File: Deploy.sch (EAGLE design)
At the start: 41 parts, among them SW5 THAU13-AB-R, SW6 THAU13-AB-R, SW7 TVAF06-A020B-R, SW8 TVAF06-A020B-R, T2 HN1C01FU, T3 HN1C01FU, U4 OPA340N, U5 DRIVER-LV8548MC-AH(SOIC10), U6 I-02247_NJM2845

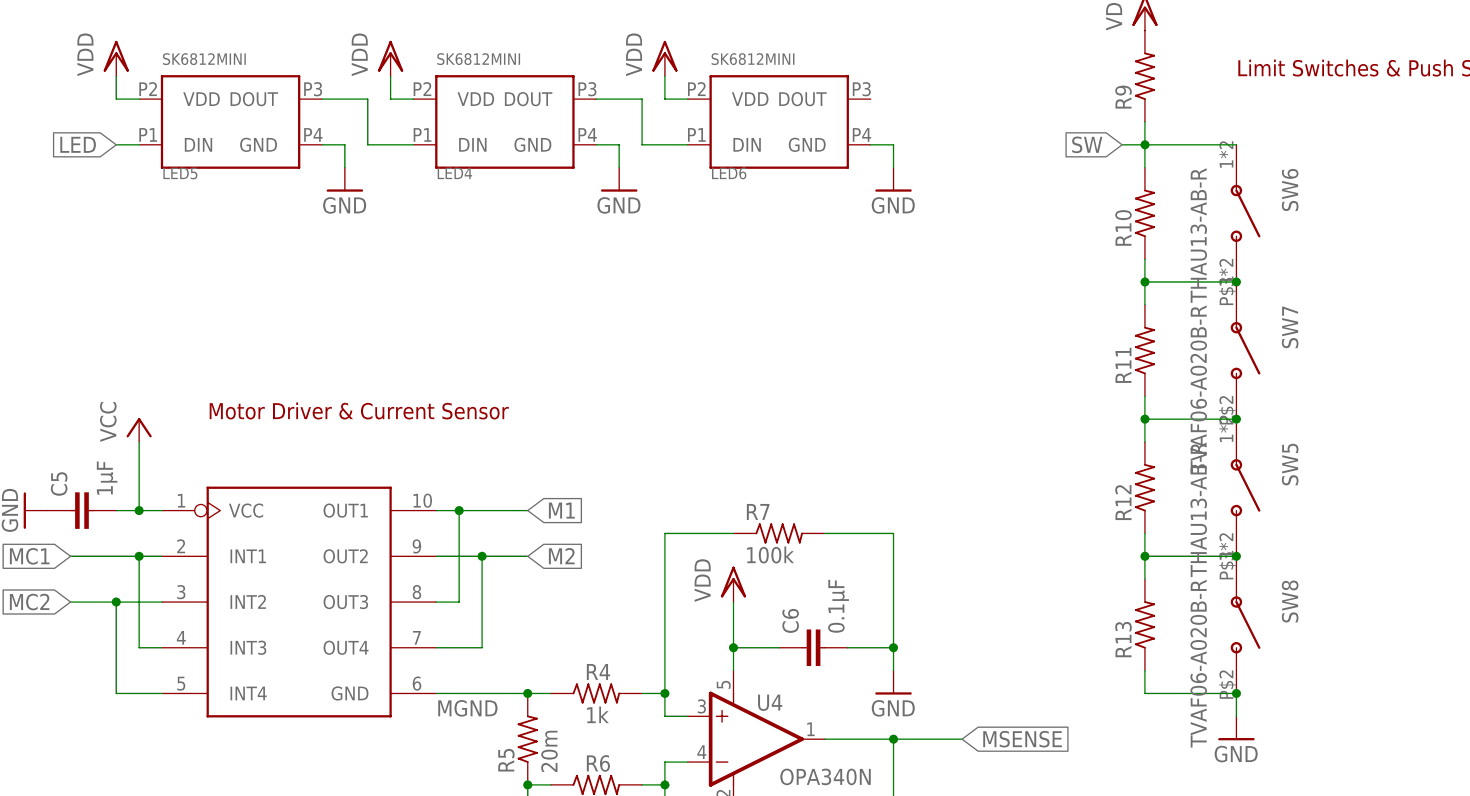
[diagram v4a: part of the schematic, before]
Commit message: Format silk
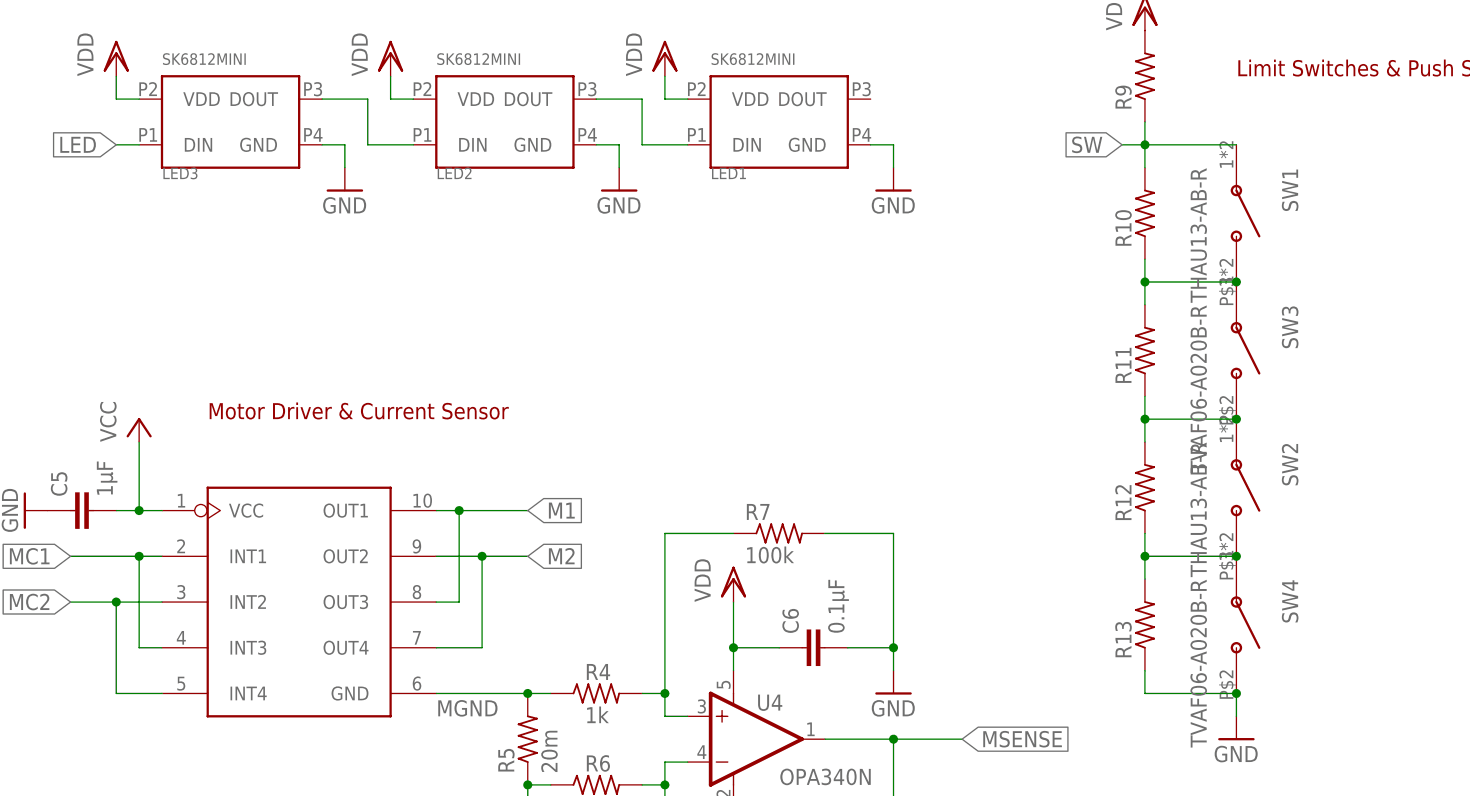
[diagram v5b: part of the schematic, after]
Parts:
- renumbered LED4 to LED2, LED5 to LED3, LED6 to LED1, SW5 to SW2, SW6 to SW1, SW7 to SW3, SW8 to SW4
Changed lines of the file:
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@@
 <part name="GND37" library="supply1" library_urn="urn:adsk.eagle:library:371" deviceset="GND" device=""/>
 <part name="R1" library="rcl" library_urn="urn:adsk.eagle:library:334" deviceset="R-US_" device="R0603" package3d_urn="urn:adsk.eagle:package:23555/3" value="100k"/>
-<part name="SW5" library="switches" deviceset="THAU13-AB-R" device=""/>
-<part name="SW6" library="switches" deviceset="THAU13-AB-R" device=""/>
+<part name="SW2" library="switches" deviceset="THAU13-AB-R" device=""/>
+<part name="SW1" library="switches" deviceset="THAU13-AB-R" device=""/>
 <part name="C4" library="rcl" library_urn="urn:adsk.eagle:library:334" deviceset="C-EU" device="C0603" package3d_urn="urn:adsk.eagle:package:23616/2" value="0.1µF"/>
 <part name="GND38" library="supply1" library_urn="urn:adsk.eagle:library:371" deviceset="GND" device=""/>
-<part name="LED4" library="leds" deviceset="SK6812MINI" device=""/>
-<part name="LED5" library="leds" deviceset="SK6812MINI" device=""/>
+<part name="LED2" library="leds" deviceset="SK6812MINI" device=""/>
+<part name="LED3" library="leds" deviceset="SK6812MINI" device=""/>
 <part name="VDD13" library="supply1" library_urn="urn:adsk.eagle:library:371" deviceset="VDD" device=""/>
 <part name="VDD14" library="supply1" library_urn="urn:adsk.eagle:library:371" deviceset="VDD" device=""/>
 <part name="GND39" library="supply1" library_urn="urn:adsk.eagle:library:371" deviceset="GND" device=""/>
 <part name="GND40" library="supply1" library_urn="urn:adsk.eagle:library:371" deviceset="GND" device=""/>
-<part name="SW7" library="switches" deviceset="TVAF06-A020B-R" device=""/>
-<part name="LED6" library="leds" deviceset="SK6812MINI" device=""/>
+<part name="SW3" library="switches" deviceset="TVAF06-A020B-R" device=""/>
+<part name="LED1" library="leds" deviceset="SK6812MINI" device=""/>
 <part name="GND41" library="supply1" library_urn="urn:adsk.eagle:library:371" deviceset="GND" device=""/>
 <part name="VDD15" library="supply1" library_urn="urn:adsk.eagle:library:371" deviceset="VDD" device=""/>
@@
 <part name="VDD16" library="supply1" library_urn="urn:adsk.eagle:library:371" deviceset="VDD" device=""/>
 <part name="GND42" library="supply1" library_urn="urn:adsk.eagle:library:371" deviceset="GND" device=""/>
-<part name="SW8" library="switches" deviceset="TVAF06-A020B-R" device=""/>
+<part name="SW4" library="switches" deviceset="TVAF06-A020B-R" device=""/>
 </parts>
 <sheets>
@@
 <attribute name="VALUE" x="69.85" y="155.702" size="1.778" layer="96" rot="R180"/>
 </instance>
-<instance part="SW5" gate="G$1" x="254" y="114.3" smashed="yes" rot="R270">
+<instance part="SW2" gate="G$1" x="254" y="114.3" smashed="yes" rot="R270">
 <attribute name="NAME" x="259.08" y="119.38" size="1.778" layer="95" rot="R270"/>
 <attribute name="VALUE" x="248.92" y="119.38" size="1.778" layer="96" rot="R270"/>
 </instance>
-<instance part="SW6" gate="G$1" x="254" y="144.78" smashed="yes" rot="R270">
+<instance part="SW1" gate="G$1" x="254" y="144.78" smashed="yes" rot="R270">
 <attribute name="NAME" x="259.08" y="149.86" size="1.778" layer="95" rot="R270"/>
 <attribute name="VALUE" x="248.92" y="149.86" size="1.778" layer="96" rot="R270"/>
@@
 <attribute name="VALUE" x="-15.24" y="55.88" size="1.778" layer="96"/>
 </instance>
-<instance part="LED4" gate="G$1" x="172.72" y="154.94" smashed="yes" rot="MR180">
+<instance part="LED2" gate="G$1" x="172.72" y="154.94" smashed="yes" rot="MR180">
 <attribute name="NAME" x="165.1" y="149.86" size="1.27" layer="95" rot="MR180"/>
 <attribute name="VALUE" x="165.1" y="162.56" size="1.27" layer="96" rot="MR180"/>
 </instance>
-<instance part="LED5" gate="G$1" x="142.24" y="154.94" smashed="yes" rot="MR180">
+<instance part="LED3" gate="G$1" x="142.24" y="154.94" smashed="yes" rot="MR180">
 <attribute name="NAME" x="134.62" y="149.86" size="1.27" layer="95" rot="MR180"/>
 <attribute name="VALUE" x="134.62" y="162.56" size="1.27" layer="96" rot="MR180"/>
@@
 <attribute name="VALUE" x="182.88" y="144.78" size="1.778" layer="96"/>
 </instance>
-<instance part="SW7" gate="G$1" x="254" y="129.54" smashed="yes" rot="R270">
+<instance part="SW3" gate="G$1" x="254" y="129.54" smashed="yes" rot="R270">
 <attribute name="NAME" x="259.08" y="134.62" size="1.778" layer="95" rot="R270"/>
 <attribute name="VALUE" x="248.92" y="134.62" size="1.778" layer="96" rot="R270"/>
 </instance>
-<instance part="LED6" gate="G$1" x="203.2" y="154.94" smashed="yes" rot="MR180">
+<instance part="LED1" gate="G$1" x="203.2" y="154.94" smashed="yes" rot="MR180">
 <attribute name="NAME" x="195.58" y="149.86" size="1.27" layer="95" rot="MR180"/>
 <attribute name="VALUE" x="195.58" y="162.56" size="1.27" layer="96" rot="MR180"/>
@@
 <attribute name="VALUE" x="251.46" y="83.82" size="1.778" layer="96"/>
 </instance>
-<instance part="SW8" gate="G$1" x="254" y="99.06" smashed="yes" rot="R270">
+<instance part="SW4" gate="G$1" x="254" y="99.06" smashed="yes" rot="R270">
 <attribute name="NAME" x="259.08" y="104.14" size="1.778" layer="95" rot="R270"/>
 <attribute name="VALUE" x="248.92" y="104.14" size="1.778" layer="96" rot="R270"/>
@@
 </segment>
 <segment>
-<pinref part="LED5" gate="G$1" pin="GND"/>
+<pinref part="LED3" gate="G$1" pin="GND"/>
 <wire x1="152.4" y1="152.4" x2="154.94" y2="152.4" width="0.1524" layer="91"/>
 <wire x1="154.94" y1="152.4" x2="154.94" y2="149.86" width="0.1524" layer="91"/>
@@
 </segment>
 <segment>
-<pinref part="LED4" gate="G$1" pin="GND"/>
+<pinref part="LED2" gate="G$1" pin="GND"/>
 <wire x1="182.88" y1="152.4" x2="185.42" y2="152.4" width="0.1524" layer="91"/>
 <wire x1="185.42" y1="152.4" x2="185.42" y2="149.86" width="0.1524" layer="91"/>
@@
 <wire x1="215.9" y1="152.4" x2="215.9" y2="149.86" width="0.1524" layer="91"/>
 <pinref part="GND41" gate="1" pin="GND"/>
-<pinref part="LED6" gate="G$1" pin="GND"/>
+<pinref part="LED1" gate="G$1" pin="GND"/>
 <wire x1="213.36" y1="152.4" x2="215.9" y2="152.4" width="0.1524" layer="91"/>
 </segment>
@@
 <wire x1="254" y1="91.44" x2="254" y2="88.9" width="0.1524" layer="91"/>
 <wire x1="243.84" y1="91.44" x2="254" y2="91.44" width="0.1524" layer="91"/>
-<pinref part="SW8" gate="G$1" pin="B"/>
+<pinref part="SW4" gate="G$1" pin="B"/>
 <junction x="254" y="91.44"/>
 <pinref part="R13" gate="G$1" pin="1"/>
@@
 </segment>
 <segment>
-<pinref part="LED4" gate="G$1" pin="VDD"/>
+<pinref part="LED2" gate="G$1" pin="VDD"/>
 <wire x1="162.56" y1="157.48" x2="160.02" y2="157.48" width="0.1524" layer="91"/>
 <wire x1="160.02" y1="157.48" x2="160.02" y2="160.02" width="0.1524" layer="91"/>
@@
 </segment>
 <segment>
-<pinref part="LED5" gate="G$1" pin="VDD"/>
+<pinref part="LED3" gate="G$1" pin="VDD"/>
 <wire x1="132.08" y1="157.48" x2="129.54" y2="157.48" width="0.1524" layer="91"/>
 <wire x1="129.54" y1="157.48" x2="129.54" y2="160.02" width="0.1524" layer="91"/>
@@
 <wire x1="190.5" y1="157.48" x2="190.5" y2="160.02" width="0.1524" layer="91"/>
 <pinref part="VDD15" gate="G$1" pin="VDD"/>
-<pinref part="LED6" gate="G$1" pin="VDD"/>
+<pinref part="LED1" gate="G$1" pin="VDD"/>
 <wire x1="190.5" y1="157.48" x2="193.04" y2="157.48" width="0.1524" layer="91"/>
 </segment>
@@
 <net name="N$22" class="0">
 <segment>
-<pinref part="LED5" gate="G$1" pin="DOUT"/>
+<pinref part="LED3" gate="G$1" pin="DOUT"/>
 <wire x1="152.4" y1="157.48" x2="157.48" y2="157.48" width="0.1524" layer="91"/>
 <wire x1="157.48" y1="157.48" x2="157.48" y2="152.4" width="0.1524" layer="91"/>
-<pinref part="LED4" gate="G$1" pin="DIN"/>
+<pinref part="LED2" gate="G$1" pin="DIN"/>
 <wire x1="157.48" y1="152.4" x2="162.56" y2="152.4" width="0.1524" layer="91"/>
 </segment>
@@
 <net name="LED" class="0">
 <segment>
-<pinref part="LED5" gate="G$1" pin="DIN"/>
+<pinref part="LED3" gate="G$1" pin="DIN"/>
 <wire x1="132.08" y1="152.4" x2="129.54" y2="152.4" width="0.1524" layer="91"/>
 <label x="129.54" y="152.4" size="1.778" layer="95" rot="R180" xref="yes"/>
@@
 <net name="N$23" class="0">
 <segment>
-<pinref part="LED4" gate="G$1" pin="DOUT"/>
+<pinref part="LED2" gate="G$1" pin="DOUT"/>
 <wire x1="182.88" y1="157.48" x2="187.96" y2="157.48" width="0.1524" layer="91"/>
 <wire x1="187.96" y1="157.48" x2="187.96" y2="152.4" width="0.1524" layer="91"/>
-<pinref part="LED6" gate="G$1" pin="DIN"/>
+<pinref part="LED1" gate="G$1" pin="DIN"/>
 <wire x1="193.04" y1="152.4" x2="187.96" y2="152.4" width="0.1524" layer="91"/>
 </segment>
@@
 <pinref part="R10" gate="G$1" pin="2"/>
 <wire x1="243.84" y1="154.94" x2="243.84" y2="152.4" width="0.1524" layer="91"/>
-<pinref part="SW6" gate="G$1" pin="A"/>
+<pinref part="SW1" gate="G$1" pin="A"/>
 <wire x1="243.84" y1="152.4" x2="243.84" y2="149.86" width="0.1524" layer="91"/>
 <wire x1="243.84" y1="152.4" x2="254" y2="152.4" width="0.1524" layer="91"/>
@@
 <pinref part="R11" gate="G$1" pin="1"/>
 <wire x1="243.84" y1="124.46" x2="243.84" y2="121.92" width="0.1524" layer="91"/>
-<pinref part="SW7" gate="G$1" pin="B"/>
-<pinref part="SW5" gate="G$1" pin="A"/>
+<pinref part="SW3" gate="G$1" pin="B"/>
+<pinref part="SW2" gate="G$1" pin="A"/>
 <wire x1="243.84" y1="121.92" x2="243.84" y2="119.38" width="0.1524" layer="91"/>
 <wire x1="243.84" y1="121.92" x2="254" y2="121.92" width="0.1524" layer="91"/>
@@
 <net name="N$25" class="0">
 <segment>
-<pinref part="SW6" gate="G$1" pin="B"/>
-<pinref part="SW7" gate="G$1" pin="A"/>
+<pinref part="SW1" gate="G$1" pin="B"/>
+<pinref part="SW3" gate="G$1" pin="A"/>
 <wire x1="254" y1="137.16" x2="243.84" y2="137.16" width="0.1524" layer="91"/>
 <junction x="254" y="137.16"/>
@@
 <pinref part="R12" gate="G$1" pin="1"/>
 <wire x1="243.84" y1="109.22" x2="243.84" y2="106.68" width="0.1524" layer="91"/>
-<pinref part="SW5" gate="G$1" pin="B"/>
+<pinref part="SW2" gate="G$1" pin="B"/>
 <wire x1="243.84" y1="106.68" x2="254" y2="106.68" width="0.1524" layer="91"/>
-<pinref part="SW8" gate="G$1" pin="A"/>
+<pinref part="SW4" gate="G$1" pin="A"/>
 <junction x="254" y="106.68"/>
 <pinref part="R13" gate="G$1" pin="2"/>
